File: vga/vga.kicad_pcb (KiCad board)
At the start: 2 copper layers, 45.2 x 59.8 mm, 29 parts, among them J1 VGA, J2 TV Interface, Q1 BC847BDW1, U1 SN74LS86ADR, U2 Pico

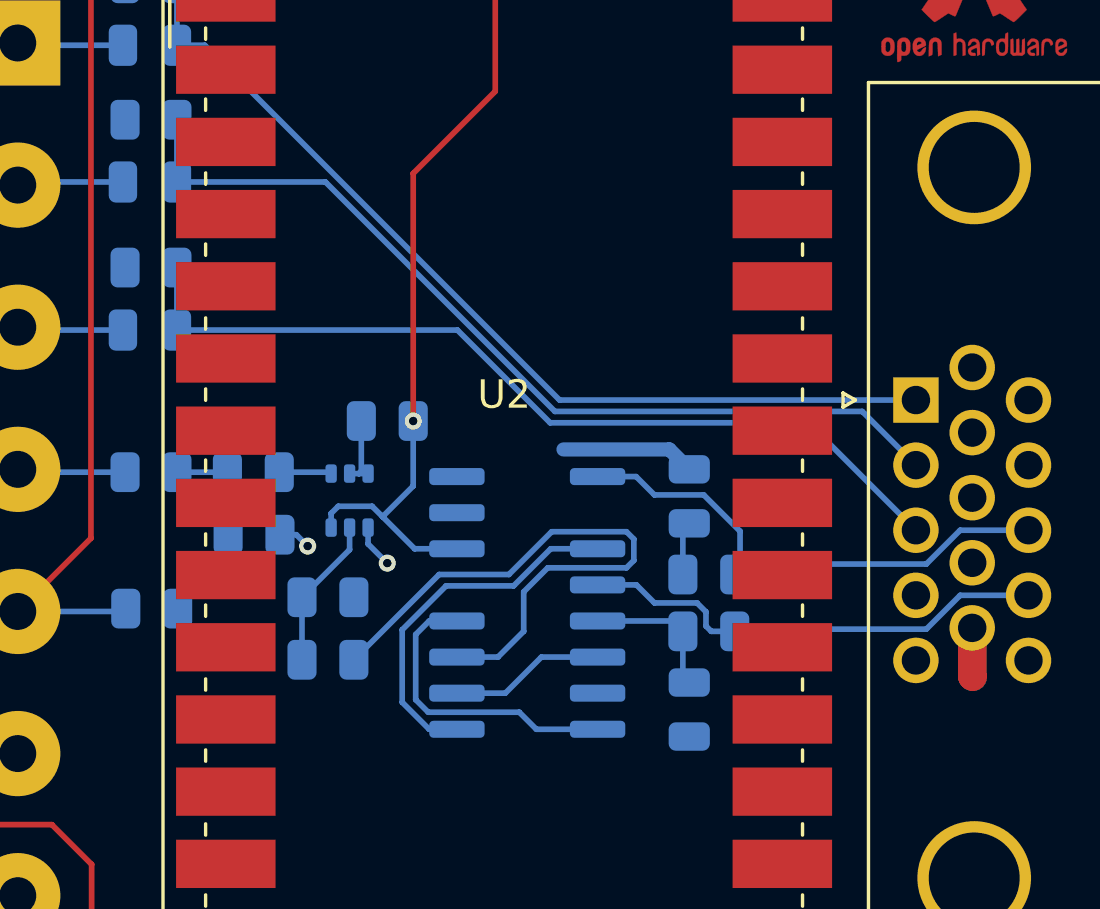
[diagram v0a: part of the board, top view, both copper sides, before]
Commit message: fix incorrect footprint in vga board; rewrite stick codebase to use pcf8575 i/o expanders and vga codebase to fix bugs and support rgb blanking
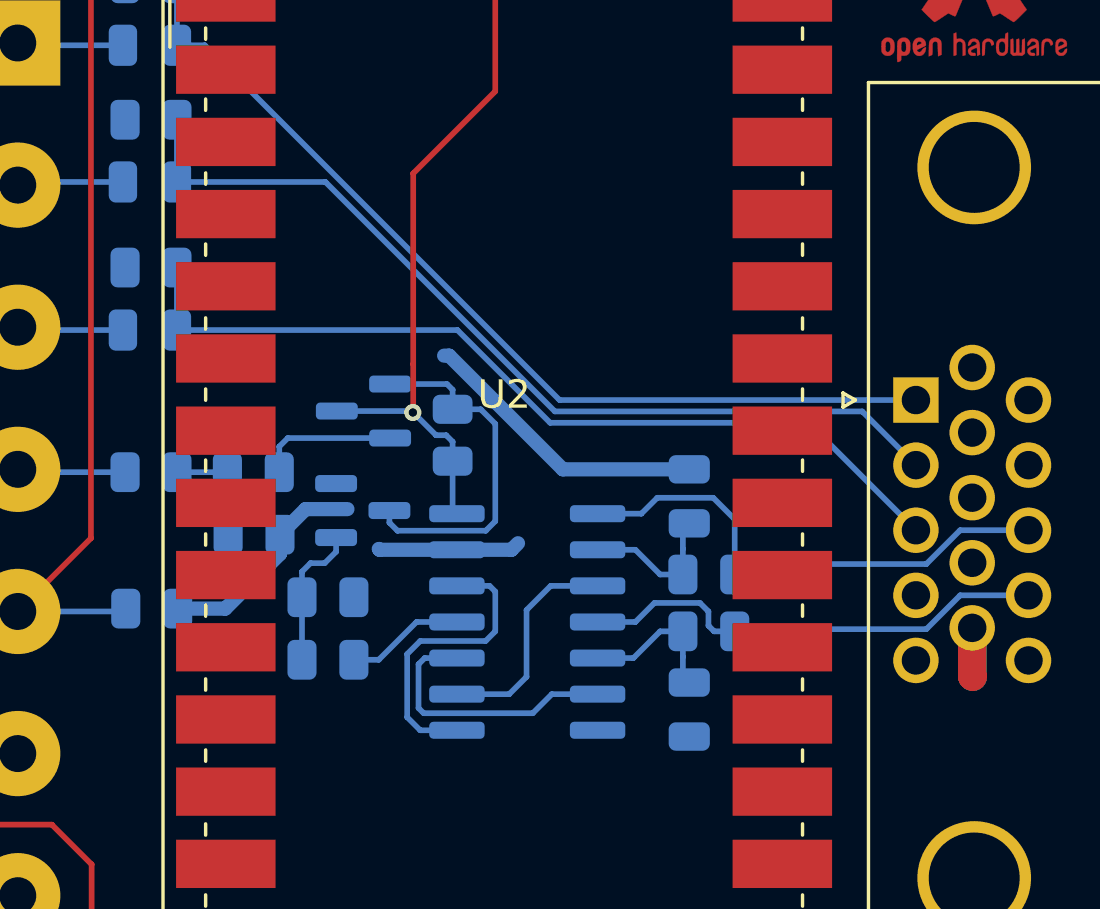
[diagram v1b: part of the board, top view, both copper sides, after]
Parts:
- added Q2: BC847, Package_TO_SOT_SMD:SOT-23, B.Cu at (92.8, 71.5)
- Q1: value BC847BDW1 -> BC847; footprint Package_TO_SOT_SMD:SOT-363_SC-70-6 -> Package_TO_SOT_SMD:SOT-23
- U1: footprint Package_SO:SOIC-14-16_3.9x9.9mm_P1.27mm -> Package_SO:SOIC-14_3.9x8.7mm_P1.27mm
- moved R5 2.35 mm to (95.9, 72.3), turned to 90 degrees
- moved U1 0.67 mm to (98.5, 78.9)
- moved Q1 0.58 mm to (92.7, 75.0), turned to 0 degrees
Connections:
- Q1 pad 1: GND -> Net-(Q1-B)
- Q1 pad 2: Net-(Q1A-B1) -> GND
- Q1 pad 3: +5V -> Net-(Q1-C)
- R3 pad 2: Net-(Q1A-B1) -> Net-(Q1-B)
- R4 pad 1: Net-(Q1A-B1) -> Net-(Q1-B)
- R5 pad 2: Net-(Q1A-C1) -> Net-(Q1-C)
- R6 pad 1: Net-(Q1B-E2) -> Net-(Q2-E)
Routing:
- net Net-(R3-Pad1): track 21.0 -> 4.18 mm
- net GND: track 10.8 -> 26.6 mm, vias 2 -> 0
- net Net-(Q1-C): track 0.00 -> 12.5 mm
- net Net-(Q1A-B1): track 5.34 -> 0.00 mm
- net Net-(Q1-B): track 0.00 -> 5.09 mm
- net Net-(U1-Pad3): track 12.9 -> 7.90 mm
- net Net-(Q2-E): track 0.00 -> 4.99 mm
- net Net-(U1-Pad10): track 5.48 -> 9.63 mm
- net Net-(C1-Pad1): track 1.89 -> 5.25 mm
- net +5V: track 39.5 -> 36.9 mm
- net Net-(Q1A-C1): track 2.54 -> 0.00 mm
- net Net-(Q1B-E2): track 1.92 -> 0.00 mm
